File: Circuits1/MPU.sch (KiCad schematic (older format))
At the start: 5 parts

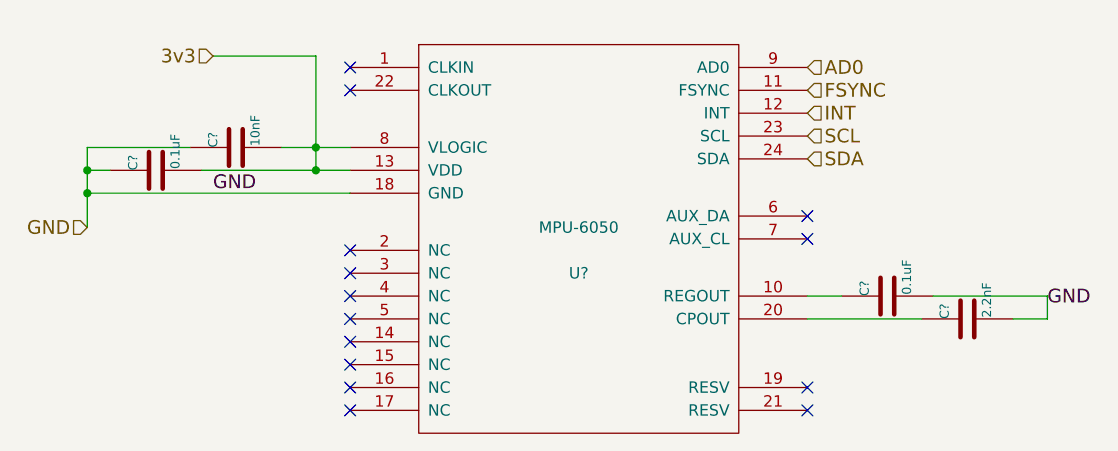
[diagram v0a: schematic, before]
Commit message: Tx Ground Planes
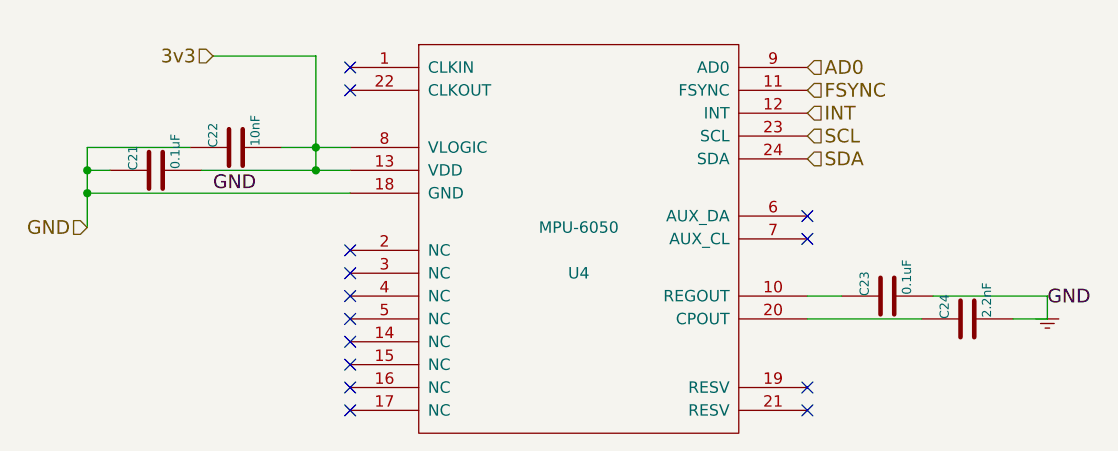
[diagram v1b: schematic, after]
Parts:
- gave numbers to parts that had none: 5
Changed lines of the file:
@@
-EESchema Schematic File Version 2  date Tuesday, 14 January 2014 21:59:12
+EESchema Schematic File Version 2
 LIBS:power
 LIBS:device
@@
 Sheet 4 4
 Title ""
-Date "14 jan 2014"
+Date "22 jan 2014"
 Rev ""
 Comp ""
@@
 $EndDescr
 $Comp
-L MPU-6050 U?
+L MPU-6050 U4
 U 1 1 52D53B00
 P 5100 3550
-F 0 "U?" H 5100 3450 50  0000 C CNN
+F 0 "U4" H 5100 3450 50  0000 C CNN
 F 1 "MPU-6050" H 5100 3650 50  0000 C CNN
 F 2 "MODULE" H 5100 3550 50  0001 C CNN
@@
 	4100 3200 3450 3200
 $Comp
-L C C?
+L C C21
 U 1 1 52D53EE0
 P 3250 3200
-F 0 "C?" H 3250 3300 40  0000 L CNN
+F 0 "C21" H 3250 3300 40  0000 L CNN
 F 1 "0.1uF" H 3256 3115 40  0000 L CNN
 F 2 "~" H 3288 3050 30  0000 C CNN
@@
 Connection ~ 2950 3300
 $Comp
-L C C?
+L C C22
 U 1 1 52D53F02
 P 3600 3100
-F 0 "C?" H 3600 3200 40  0000 L CNN
+F 0 "C22" H 3600 3200 40  0000 L CNN
 F 1 "10nF" H 3606 3015 40  0000 L CNN
 F 2 "~" H 3638 2950 30  0000 C CNN
@@
 Connection ~ 3950 3200
 $Comp
-L C C?
+L C C23
 U 1 1 52D53F2F
 P 6450 3750
-F 0 "C?" H 6450 3850 40  0000 L CNN
+F 0 "C23" H 6450 3850 40  0000 L CNN
 F 1 "0.1uF" H 6456 3665 40  0000 L CNN
 F 2 "~" H 6488 3600 30  0000 C CNN
@@
 	6100 3750 6250 3750
 $Comp
-L C C?
+L C C24
 U 1 1 52D53F47
 P 6800 3850
-F 0 "C?" H 6800 3950 40  0000 L CNN
+F 0 "C24" H 6800 3950 40  0000 L CNN
 F 1 "2.2nF" H 6806 3765 40  0000 L CNN
 F 2 "~" H 6838 3700 30  0000 C CNN
@@
 Text HLabel 6100 3150 2    60   Input ~ 0
 SDA
+$Comp
+L GND #PWR063
+U 1 1 52DE84BB
+P 7150 3850
+F 0 "#PWR063" H 7150 3850 30  0001 C CNN
+F 1 "GND" H 7150 3780 30  0001 C CNN
+F 2 "" H 7150 3850 60  0000 C CNN
+F 3 "" H 7150 3850 60  0000 C CNN
+	1    7150 3850
+	1    0    0    -1
+$EndComp
 $EndSCHEMATC

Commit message: Neatened Schematics and Final PCB
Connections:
- net 3v3 renamed 3V3
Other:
- moved on the sheet: C21, C22, C24
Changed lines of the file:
@@
 Sheet 4 4
 Title ""
-Date "22 jan 2014"
+Date "7 mar 2014"
 Rev ""
 Comp ""
@@
 NoConn ~ 6100 4250
 NoConn ~ 6100 4150
-Wire Wire Line
-	2950 3300 4100 3300
-Text HLabel 3500 2700 0    60   Input ~ 0
+Text HLabel 3100 2700 0    60   Input ~ 0
 3v3
-Text HLabel 2950 3450 0    60   Input ~ 0
+Text HLabel 3100 3300 0    60   Input ~ 0
 GND
 NoConn ~ 6100 3400
 NoConn ~ 6100 3500
-Wire Wire Line
-	4100 3200 3450 3200
 $Comp
 L C C21
 U 1 1 52D53EE0
-P 3250 3200
-F 0 "C21" H 3250 3300 40  0000 L CNN
-F 1 "0.1uF" H 3256 3115 40  0000 L CNN
-F 2 "~" H 3288 3050 30  0000 C CNN
-F 3 "~" H 3250 3200 60  0000 C CNN
-	1    3250 3200
+P 3600 3200
+F 0 "C21" H 3600 3300 40  0000 L CNN
+F 1 "0.1uF" H 3606 3115 40  0000 L CNN
+F 2 "~" H 3638 3050 30  0000 C CNN
+F 3 "~" H 3600 3200 60  0000 C CNN
+	1    3600 3200
 	0    -1   -1   0
 $EndComp
-Wire Wire Line
-	2950 3100 2950 3450
-Wire Wire Line
-	3050 3200 2950 3200
-Connection ~ 2950 3300
 $Comp
 L C C22
 U 1 1 52D53F02
-P 3600 3100
-F 0 "C22" H 3600 3200 40  0000 L CNN
-F 1 "10nF" H 3606 3015 40  0000 L CNN
-F 2 "~" H 3638 2950 30  0000 C CNN
-F 3 "~" H 3600 3100 60  0000 C CNN
-	1    3600 3100
+P 3600 2950
+F 0 "C22" H 3600 3050 40  0000 L CNN
+F 1 "10nF" H 3606 2865 40  0000 L CNN
+F 2 "~" H 3638 2800 30  0000 C CNN
+F 3 "~" H 3600 2950 60  0000 C CNN
+	1    3600 2950
 	0    -1   -1   0
 $EndComp
 Wire Wire Line
 	4100 3100 3800 3100
-Wire Wire Line
-	3400 3100 2950 3100
-Connection ~ 2950 3200
-Wire Wire Line
-	3500 2700 3950 2700
-Wire Wire Line
-	3950 2700 3950 3200
-Connection ~ 3950 3100
-Connection ~ 3950 3200
 $Comp
 L C C23
@@
 L C C24
 U 1 1 52D53F47
-P 6800 3850
-F 0 "C24" H 6800 3950 40  0000 L CNN
-F 1 "2.2nF" H 6806 3765 40  0000 L CNN
-F 2 "~" H 6838 3700 30  0000 C CNN
-F 3 "~" H 6800 3850 60  0000 C CNN
-	1    6800 3850
+P 6450 3950
+F 0 "C24" H 6450 4050 40  0000 L CNN
+F 1 "2.2nF" H 6456 3865 40  0000 L CNN
+F 2 "~" H 6488 3800 30  0000 C CNN
+F 3 "~" H 6450 3950 60  0000 C CNN
+	1    6450 3950
 	0    -1   -1   0
 $EndComp
-Wire Wire Line
-	6100 3850 6600 3850
-Wire Wire Line
-	6650 3750 7150 3750
-Wire Wire Line
-	7150 3750 7150 3850
-Wire Wire Line
-	7150 3850 7000 3850
-Text Label 3500 3300 0    60   ~ 0
-GND
-Text Label 7150 3800 0    60   ~ 0
-GND
 Text HLabel 6100 2750 2    60   Input ~ 0
 AD0
@@
 Text HLabel 6100 3150 2    60   Input ~ 0
 SDA
+Wire Wire Line
+	3800 2700 3800 3200
+Wire Wire Line
+	3800 3200 4100 3200
+Connection ~ 3800 2950
+Wire Wire Line
+	3100 2700 3800 2700
+Wire Wire Line
+	3400 3200 3300 3200
+Connection ~ 3300 3300
+Wire Wire Line
+	3300 2950 3400 2950
+Connection ~ 3300 3200
+Connection ~ 3800 3100
+Connection ~ 3800 3200
+Wire Wire Line
+	3100 3300 4100 3300
+Wire Wire Line
+	6100 3850 6250 3850
+Wire Wire Line
+	6250 3850 6250 3950
+Wire Wire Line
+	6650 3950 6750 3950
+Connection ~ 6750 3950
+Wire Wire Line
+	6650 3750 6750 3750
 $Comp
-L GND #PWR063
-U 1 1 52DE84BB
-P 7150 3850
-F 0 "#PWR063" H 7150 3850 30  0001 C CNN
-F 1 "GND" H 7150 3780 30  0001 C CNN
-F 2 "" H 7150 3850 60  0000 C CNN
-F 3 "" H 7150 3850 60  0000 C CNN
-	1    7150 3850
+L GND #PWR?
+U 1 1 531AA3FE
+P 6750 4050
+F 0 "#PWR?" H 6750 4050 30  0001 C CNN
+F 1 "GND" H 6750 3980 30  0001 C CNN
+F 2 "" H 6750 4050 60  0000 C CNN
+F 3 "" H 6750 4050 60  0000 C CNN
+	1    6750 4050
 	1    0    0    -1
 $EndComp
+Wire Wire Line
+	6750 3750 6750 4050
+Wire Wire Line
+	3300 2950 3300 3400
+$Comp
+L GND #PWR?
+U 1 1 531AA437
+P 3300 3400
+F 0 "#PWR?" H 3300 3400 30  0001 C CNN
+F 1 "GND" H 3300 3330 30  0001 C CNN
+F 2 "" H 3300 3400 60  0000 C CNN
+F 3 "" H 3300 3400 60  0000 C CNN
+	1    3300 3400
+	1    0    0    -1
+$EndComp
+$Comp
+L 3V3 #PWR?
+U 1 1 531AA446
+P 3300 2700
+F 0 "#PWR?" H 3300 2800 40  0001 C CNN
+F 1 "3V3" H 3300 2825 40  0000 C CNN
+F 2 "" H 3300 2700 60  0000 C CNN
+F 3 "" H 3300 2700 60  0000 C CNN
+	1    3300 2700
+	1    0    0    -1
+$EndComp
+Connection ~ 3300 2700
 $EndSCHEMATC
